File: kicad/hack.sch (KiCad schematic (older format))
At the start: 27 parts, among them P1 USB_micro, P2 CONN_01X13, P3 CONN_01X13, U1 NCP1117, U2 STF202, U3 ATSAMD21E, U4 MRF24J40MA, X1 MC-306

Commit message: Final components placement almost done
During this phase I checked if everything could fit in the board. It
didn't, so I found a replacement LDO (in a small 1.2x1.2mm DFN package)
that needs 2x0603 ceramic caps rather than two clunky electros (more
free space then) and I finally changed the D21E package to QFN as well,
now everything seems to fit quite well.
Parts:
- removed C1, C2: 10u, Capacitors_Tantalum_SMD:TantalC_SizeA_EIA-3216_HandSoldering, symbol CP_Small
- removed U1: NCP1117, hack-footprints:SOT-223, symbol NCP1117
- removed U4: MRF24J40MA, hack-footprints:MRF24J40MA, symbol MRF24J40MA
- added C1, C2: 2.2u, Capacitors_SMD:C_0603_HandSoldering, symbol C_Small
- added U1: MIC5528, Housings_DFN_QFN:DFN-6-1EP_1.2x1.2mm_Pitch0.4mm, symbol MIC5528
- C3, C4: footprint Capacitors_Tantalum_SMD:TantalC_SizeA_EIA-3216_HandSoldering -> Capacitors_SMD:c_elec_3x5.3
- U3: footprint Housings_QFP:TQFP-32_7x7mm_Pitch0.8mm -> Housings_DFN_QFN:QFN-32-1EP_5x5mm_Pitch0.5mm
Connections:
- net labels added: USB-D+, USB-D-, VDDANA, VDDCORE, shield
- net labels removed: USB-DM, USB-DP
- no-connect marks 0 -> 1
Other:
- moved on the sheet: C10, C11, C4, C6, C7, L1, L2, P2, P3, R3, R4, S1

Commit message: Layout 99,9% finished
Nets 100% routed, need to double check if copper pours are all connected
to ground; added fiducials on board (for pick-n-place machines), I only
need to find a good spot for them
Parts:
- added FID1, FID2, FID3: FIDUCIAL, hack-footprints:FIDUCIAL, symbol FIDUCIAL
- added JP1: Jumper_NO_Small, hack-footprints:SMD_Jumper, symbol Jumper_NO_Small
- added P4: CONN_01X01, Pin_Headers:Pin_Header_Straight_1x01, symbol CONN_01X01
- D1: footprint Resistors_SMD:R_0603_HandSoldering -> hack-footprints:LED_0603_HandSoldering
- L1: footprint Resistors_SMD:R_0603_HandSoldering -> hack-footprints:L_0603_HandSoldering
- U1: footprint Housings_DFN_QFN:DFN-6-1EP_1.2x1.2mm_Pitch0.4mm -> hack-footprints:DFN-6-1EP_1.2x1.2mm_Pitch0.4mm
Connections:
- net labels added: VLDO
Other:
- moved on the sheet: P2, P3

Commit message: Cleaning up before test run
Removed obsolete Eagle CAD files, added OSHW/Hackaday logos on schematic
and silkscreen, removed ground connections for pins 2-3 of 32.768 KHz
XTAL, removed traces under USB data lines, moving analog lines around
(not beneath) XTAL (w.i.p.), moved components names on silkscreen to be
readable, set fiducials in position, fixed SPST SMD package
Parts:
- added LOGO1: OSHW, hack-footprints:OSHW-LOGO, symbol OSHW
- added LOGO2: HACKADAY, hack-footprints:HACKADAY-LOGO, symbol HACKADAY
- C3, C4: footprint Capacitors_SMD:c_elec_3x5.3 -> hack-footprints:c_elec_3x5.3
- S1: footprint Buttons_Switches_SMD:SW_SPST_EVQP2 -> hack-footprints:SPST
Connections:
- wire segments 89 -> 87
- no-connect marks 1 -> 4
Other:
- moved on the sheet: C1, C10, C11, C2, C3, C4, C5, C6, C7, C8, C9, D1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

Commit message: Layout 100% completed, cosmetics not yet
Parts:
- removed X1: MC-306, hack-footprints:MC-306, symbol MC-306
- added LOGO3: HACK, hack-footprints:HACK-LOGO, symbol HACK
- added X1: ABS07, hack-footprints:xtal_3.2x1.5mm, symbol ABS07
- C6, C7: value 15p -> 10p
- S1: footprint hack-footprints:SPST -> hack-footprints:SPST-PTS_810
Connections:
- net labels added: PA02/A0, PA03/A1, PA04/A2, PA05/A3, PA06/A4, PA07/A5, PA08/0, PA09/1, PA10/2, PA11/3, PA14/4, PA15/5, PA16/6, PA17/7, PA18/8, PA19/9, PA22/10, PA23/11, PA27/12, PA28/13
- net labels removed: PA02/A, PA03/A, PA04/A, PA05/A, PA06/A, PA07/A, PA08, PA09, PA10, PA11, PA14, PA15, PA16, PA17, PA18, PA19, PA22, PA23, PA27, PA28
- wire segments 87 -> 88
- no-connect marks 4 -> 2
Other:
- moved on the sheet: R4, S1
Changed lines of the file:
@@
 LIBS:HACK
 LIBS:HiFiAudioCodecModule-cache
+LIBS:hack logo
 LIBS:hack-cache
 EELAYER 25 0
@@
 $EndComp
 $Comp
-L MC-306 X1
-U 1 1 56571094
-P 2150 1800
-F 0 "X1" H 2150 1650 60  0000 C CNN
-F 1 "MC-306" H 2150 1850 60  0000 C CNN
-F 2 "hack-footprints:MC-306" H 2150 1800 60  0001 C CNN
-F 3 "" H 2150 1800 60  0000 C CNN
-	1    2150 1800
-	1    0    0    -1
-$EndComp
-$Comp
 L R_Small R1
 U 1 1 565719DA
@@
 P 1800 2100
 F 0 "C6" H 1810 2170 50  0000 L CNN
-F 1 "15p" H 1810 2020 50  0000 L CNN
+F 1 "10p" H 1810 2020 50  0000 L CNN
 F 2 "Capacitors_SMD:C_0603_HandSoldering" H 1800 2100 60  0001 C CNN
 F 3 "" H 1800 2100 60  0000 C CNN
@@
 P 2500 2100
 F 0 "C7" H 2510 2170 50  0000 L CNN
-F 1 "15p" H 2510 2020 50  0000 L CNN
+F 1 "10p" H 2510 2020 50  0000 L CNN
 F 2 "Capacitors_SMD:C_0603_HandSoldering" H 2500 2100 60  0001 C CNN
 F 3 "" H 2500 2100 60  0000 C CNN
@@
 L R_Small R4
 U 1 1 56589A59
-P 6150 1850
-F 0 "R4" H 6180 1870 50  0000 L CNN
-F 1 "330" H 6180 1810 50  0000 L CNN
-F 2 "Resistors_SMD:R_0603_HandSoldering" H 6150 1850 60  0001 C CNN
-F 3 "" H 6150 1850 60  0000 C CNN
-	1    6150 1850
+P 6175 1850
+F 0 "R4" H 6205 1870 50  0000 L CNN
+F 1 "330" H 6205 1810 50  0000 L CNN
+F 2 "Resistors_SMD:R_0603_HandSoldering" H 6175 1850 60  0001 C CNN
+F 3 "" H 6175 1850 60  0000 C CNN
+	1    6175 1850
 	-1   0    0    -1
 $EndComp
@@
 L SPST-M S1
 U 1 1 5658420D
-P 6150 2150
-F 0 "S1" V 6150 2150 60  0000 C CNN
-F 1 "SPST-M" V 5950 2150 60  0001 C CNN
-F 2 "hack-footprints:SPST" H 6150 2150 60  0001 C CNN
-F 3 "" H 6150 2150 60  0000 C CNN
-	1    6150 2150
+P 6175 2150
+F 0 "S1" V 6175 2275 60  0000 C CNN
+F 1 "SPST-M" V 5975 2150 60  0001 C CNN
+F 2 "hack-footprints:SPST-PTS_810" H 6175 2150 60  0001 C CNN
+F 3 "" H 6175 2150 60  0000 C CNN
+	1    6175 2150
 	0    1    -1   0
 $EndComp
@@
 L GND #PWR05
 U 1 1 56587427
-P 5900 2350
-F 0 "#PWR05" H 5900 2100 50  0001 C CNN
-F 1 "GND" H 5900 2200 50  0000 C CNN
-F 2 "" H 5900 2350 60  0000 C CNN
-F 3 "" H 5900 2350 60  0000 C CNN
-	1    5900 2350
+P 5900 2400
+F 0 "#PWR05" H 5900 2150 50  0001 C CNN
+F 1 "GND" H 5900 2250 50  0000 C CNN
+F 2 "" H 5900 2400 60  0000 C CNN
+F 3 "" H 5900 2400 60  0000 C CNN
+	1    5900 2400
 	-1   0    0    -1
 $EndComp
@@
 	1    0    0    -1
 $EndComp
-Text GLabel 4850 1550 2    60   BiDi ~ 0
-PA28
-Text GLabel 5400 1750 2    60   BiDi ~ 0
-PA27
-Text GLabel 6200 1650 2    60   BiDi ~ 0
+Text GLabel 5375 1550 2    60   BiDi ~ 0
+PA28/13
+Text GLabel 4850 1750 2    60   BiDi ~ 0
+PA27/12
+Text GLabel 6225 1650 2    60   BiDi ~ 0
 !RESET
 Text GLabel 4850 2050 2    60   BiDi ~ 0
-PA23
+PA23/11
 Text GLabel 4850 2150 2    60   BiDi ~ 0
-PA22
+PA22/10
 Text GLabel 4850 2250 2    60   BiDi ~ 0
-PA19
+PA19/9
 Text GLabel 4850 2350 2    60   BiDi ~ 0
-PA18
+PA18/8
 Text GLabel 4850 2450 2    60   BiDi ~ 0
-PA17
+PA17/7
 Text GLabel 4850 2550 2    60   BiDi ~ 0
-PA16
+PA16/6
 Text GLabel 4850 850  2    60   BiDi ~ 0
 PA31/SWDIO
@@
 PA30/SWCLK
 Text GLabel 3250 2550 0    60   BiDi ~ 0
-PA15
+PA15/5
 Text GLabel 3250 2450 0    60   BiDi ~ 0
-PA14
+PA14/4
 Text GLabel 3250 2350 0    60   BiDi ~ 0
-PA11
+PA11/3
 Text GLabel 3250 2250 0    60   BiDi ~ 0
-PA10
+PA10/2
 Text GLabel 3250 2150 0    60   BiDi ~ 0
-PA09
+PA09/1
 Text GLabel 3200 2050 0    60   BiDi ~ 0
-PA08
+PA08/0
 Text GLabel 3250 1050 0    60   BiDi ~ 0
-PA02/A
+PA02/A0
 Text GLabel 3250 1150 0    60   BiDi ~ 0
-PA03/A
+PA03/A1
 Text GLabel 3250 1250 0    60   BiDi ~ 0
-PA04/A
+PA04/A2
 Text GLabel 3250 1350 0    60   BiDi ~ 0
-PA05/A
+PA05/A3
 Text GLabel 3250 1450 0    60   BiDi ~ 0
-PA06/A
+PA06/A4
 Text GLabel 3250 1550 0    60   BiDi ~ 0
-PA07/A
+PA07/A5
 $Comp
 L GND #PWR07
@@
 	5350 2300 5350 2350
 Wire Wire Line
-	6150 2300 5900 2300
-Wire Wire Line
-	5900 2250 5900 2350
+	6175 2350 5900 2350
+Wire Wire Line
+	5900 2250 5900 2400
 Wire Wire Line
 	5900 1600 5900 2050
 Connection ~ 5900 1650
-Connection ~ 5900 2300
-Wire Wire Line
-	4800 1550 4850 1550
-Wire Wire Line
-	4800 1750 5400 1750
+Connection ~ 5900 2350
+Wire Wire Line
+	4800 1550 5375 1550
+Wire Wire Line
+	4800 1750 4850 1750
 Wire Wire Line
 	4800 2050 4850 2050
@@
 	5900 1325 5900 1400
 Wire Wire Line
-	4800 1650 6200 1650
-Wire Wire Line
-	6150 1950 6150 2000
-Wire Wire Line
-	6150 1650 6150 1750
-Connection ~ 6150 1650
+	4800 1650 6225 1650
+Wire Wire Line
+	6175 1950 6175 2000
+Wire Wire Line
+	6175 1650 6175 1750
+Connection ~ 6175 1650
 Wire Wire Line
 	4800 1450 5100 1450
@@
 Text GLabel 1275 3000 0    60   Output ~ 0
 VDDF
+Text GLabel 2125 3600 0    60   BiDi ~ 0
+PA17/7
+Text GLabel 2125 3700 0    60   BiDi ~ 0
+PA18/8
+Text GLabel 2125 3800 0    60   BiDi ~ 0
+PA19/9
+Text GLabel 2125 3900 0    60   BiDi ~ 0
+PA22/10
+Text GLabel 2125 4000 0    60   BiDi ~ 0
+PA23/11
 Text GLabel 1275 3100 0    60   BiDi ~ 0
-PA17
-Text GLabel 1275 3200 0    60   BiDi ~ 0
-PA18
+PA27/12
+Text GLabel 1275 3200 0    60   Input ~ 0
+!RESET
 Text GLabel 1275 3300 0    60   BiDi ~ 0
-PA19
+PA28/13
 Text GLabel 1275 3400 0    60   BiDi ~ 0
-PA22
+PA30/SWCLK
 Text GLabel 1275 3500 0    60   BiDi ~ 0
-PA23
-Text GLabel 1275 3600 0    60   BiDi ~ 0
-PA27
-Text GLabel 1275 3700 0    60   Input ~ 0
-!RESET
-Text GLabel 1275 3800 0    60   BiDi ~ 0
-PA28
-Text GLabel 1275 3900 0    60   BiDi ~ 0
-PA30/SWCLK
-Text GLabel 1275 4000 0    60   BiDi ~ 0
 PA31/SWDIO
-Wire Wire Line
-	5350 1850 5350 1750
-Connection ~ 5350 1750
 $Comp
 L CONN_01X01 P4
@@
 Text GLabel 2300 950  2    60   Output ~ 0
 USB-D-
+Text GLabel 1275 3600 0    60   BiDi ~ 0
+PA02/A0
+Text GLabel 1275 3700 0    60   BiDi ~ 0
+PA03/A1
+Text GLabel 1275 3800 0    60   BiDi ~ 0
+PA04/A2
+Text GLabel 1275 3900 0    60   BiDi ~ 0
+PA05/A3
+Text GLabel 1275 4000 0    60   BiDi ~ 0
+PA06/A4
 Text GLabel 2125 2800 0    60   BiDi ~ 0
-PA02/A
+PA07/A5
+Text GLabel 2125 3400 0    60   BiDi ~ 0
+PA15/5
+Text GLabel 2125 3300 0    60   BiDi ~ 0
+PA14/4
+Text GLabel 2125 3200 0    60   BiDi ~ 0
+PA11/3
+Text GLabel 2125 3100 0    60   BiDi ~ 0
+PA10/2
+Text GLabel 2125 3000 0    60   BiDi ~ 0
+PA09/1
 Text GLabel 2125 2900 0    60   BiDi ~ 0
-PA03/A
-Text GLabel 2125 3000 0    60   BiDi ~ 0
-PA04/A
-Text GLabel 2125 3100 0    60   BiDi ~ 0
-PA05/A
-Text GLabel 2125 3200 0    60   BiDi ~ 0
-PA06/A
-Text GLabel 2125 3300 0    60   BiDi ~ 0
-PA07/A
-Text GLabel 2125 3900 0    60   BiDi ~ 0
-PA15
-Text GLabel 2125 3800 0    60   BiDi ~ 0
-PA14
-Text GLabel 2125 3700 0    60   BiDi ~ 0
-PA11
-Text GLabel 2125 3600 0    60   BiDi ~ 0
-PA10
+PA08/0
 Text GLabel 2125 3500 0    60   BiDi ~ 0
-PA09
-Text GLabel 2125 3400 0    60   BiDi ~ 0
-PA08
-Text GLabel 2125 4000 0    60   BiDi ~ 0
-PA16
+PA16/6
 Text GLabel 1275 4225 0    60   Output ~ 0
 VDDANA
@@
 	1    0    0    -1
 $EndComp
-NoConn ~ 2050 2150
-NoConn ~ 2250 2150
 NoConn ~ 1350 1150
 $Comp
 L OSHW LOGO1
 U 1 1 56815E8B
-P 4475 3400
-F 0 "LOGO1" H 4475 3060 60  0001 C CNN
-F 1 "OSHW" H 4475 3740 60  0001 C CNN
-F 2 "hack-footprints:OSHW-LOGO" H 4475 3400 60  0001 C CNN
-F 3 "" H 4475 3400 60  0000 C CNN
-	1    4475 3400
+P 5800 3750
+F 0 "LOGO1" H 5800 3410 60  0001 C CNN
+F 1 "OSHW" H 5800 4090 60  0001 C CNN
+F 2 "hack-footprints:OSHW-LOGO" H 5800 3750 60  0001 C CNN
+F 3 "" H 5800 3750 60  0000 C CNN
+	1    5800 3750
 	1    0    0    -1
 $EndComp
@@
 L HACKADAY LOGO2
 U 1 1 56815EDD
-P 5325 3300
-F 0 "LOGO2" H 5325 3118 60  0001 C CNN
-F 1 "HACKADAY" H 5325 3482 60  0001 C CNN
-F 2 "hack-footprints:HACKADAY-LOGO" H 5325 3300 60  0001 C CNN
-F 3 "" H 5325 3300 60  0000 C CNN
-	1    5325 3300
-	1    0    0    -1
-$EndComp
+P 4450 3725
+F 0 "LOGO2" H 4450 3543 60  0001 C CNN
+F 1 "HACKADAY" H 4450 3907 60  0001 C CNN
+F 2 "hack-footprints:HACKADAY-LOGO" H 4450 3725 60  0001 C CNN
+F 3 "" H 4450 3725 60  0000 C CNN
+	1    4450 3725
+	1    0    0    -1
+$EndComp
+$Comp
+L ABS07 X1
+U 1 1 56825CA1
+P 2150 1800
+F 0 "X1" H 2150 1650 60  0000 C CNN
+F 1 "ABS07" H 2150 1850 60  0000 C CNN
+F 2 "hack-footprints:xtal_3.2x1.5mm" H 2150 1800 60  0001 C CNN
+F 3 "" H 2150 1800 60  0000 C CNN
+	1    2150 1800
+	1    0    0    -1
+$EndComp
+$Comp
+L HACK LOGO3
+U 1 1 56825DB6
+P 5125 3125
+F 0 "LOGO3" H 5125 2905 60  0001 C CNN
+F 1 "HACK" H 5125 3345 60  0001 C CNN
+F 2 "hack-footprints:HACK-LOGO" H 5125 3125 60  0001 C CNN
+F 3 "" H 5125 3125 60  0000 C CNN
+	1    5125 3125
+	1    0    0    -1
+$EndComp
+Wire Wire Line
+	6175 2350 6175 2300
+Wire Wire Line
+	5350 1850 5350 1550
+Connection ~ 5350 1550
 $EndSCHEMATC

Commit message: Changed USB connector package, revised layout
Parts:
- P1: footprint hack-footprints:47346-0001 -> hack-footprints:ST-USB-001G
- P2, P3: footprint Pin_Headers:Pin_Header_Straight_1x13 -> hack-footprints:Pin_Castellated_1x13
- P4: footprint Pin_Headers:Pin_Header_Straight_1x01 -> hack-footprints:Pin_Castellated_1x01
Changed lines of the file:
@@
 F 0 "P1" H 950 750 60  0000 C CNN
 F 1 "USB_micro" H 950 650 60  0000 C CNN
-F 2 "hack-footprints:47346-0001" H 950 700 60  0001 C CNN
+F 2 "hack-footprints:ST-USB-001G" H 950 700 60  0001 C CNN
 F 3 "" H 950 700 60  0000 C CNN
 	1    950  700
@@
 F 0 "P2" H 1475 4100 50  0000 C CNN
 F 1 "CONN_01X13" V 1575 3400 50  0000 C CNN
-F 2 "Pin_Headers:Pin_Header_Straight_1x13" H 1475 3400 60  0001 C CNN
+F 2 "hack-footprints:Pin_Castellated_1x13" H 1475 3400 60  0001 C CNN
 F 3 "" H 1475 3400 60  0000 C CNN
 	1    1475 3400
@@
 F 0 "P3" H 2325 4100 50  0000 C CNN
 F 1 "CONN_01X13" V 2425 3400 50  0000 C CNN
-F 2 "Pin_Headers:Pin_Header_Straight_1x13" H 2325 3400 60  0001 C CNN
+F 2 "hack-footprints:Pin_Castellated_1x13" H 2325 3400 60  0001 C CNN
 F 3 "" H 2325 3400 60  0000 C CNN
 	1    2325 3400
@@
 F 0 "P4" H 1475 4325 50  0000 C CNN
 F 1 "CONN_01X01" V 1575 4225 50  0000 C CNN
-F 2 "Pin_Headers:Pin_Header_Straight_1x01" H 1475 4225 60  0001 C CNN
+F 2 "hack-footprints:Pin_Castellated_1x01" H 1475 4225 60  0001 C CNN
 F 3 "" H 1475 4225 60  0000 C CNN
 	1    1475 4225

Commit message: fresh PDF and Gerbers in separate folders. Step/VRML files ready for 3D render
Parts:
- C1, C2: value 2.2u -> 2.2uF; footprint Capacitors_SMD:C_0603_HandSoldering -> hack:C_0603_HandSoldering
- C10, C11, C8, C9: value 100n -> 100nF; footprint Capacitors_SMD:C_0603_HandSoldering -> hack:C_0603_HandSoldering
- C3, C4: value 10u -> 10uF; footprint hack-footprints:c_elec_3x5.3 -> hack:c_elec_3x5.3
- C5: value 4.5n -> 4.5nF; footprint Capacitors_SMD:C_0603_HandSoldering -> hack:C_0603_HandSoldering
- C6, C7: value 10p -> 10pF; footprint Capacitors_SMD:C_0603_HandSoldering -> hack:C_0603_HandSoldering
- D1: footprint hack-footprints:LED_0603_HandSoldering -> hack:LED_0603_HandSoldering
- FID1, FID2, FID3: footprint hack-footprints:FIDUCIAL -> hack:FIDUCIAL
- JP1: footprint hack-footprints:SMD_Jumper -> hack:SMD_Jumper
- L1: footprint hack-footprints:L_0603_HandSoldering -> hack:L_0603_HandSoldering
- L2: value 10u -> 10uH; footprint hack-footprints:ELLVFG -> hack:ELLVFG
- LOGO1: footprint hack-footprints:OSHW-LOGO -> hack:OSHW-LOGO; manf# (none) -> mfr_pn
- LOGO2: footprint hack-footprints:HACKADAY-LOGO -> hack:HACKADAY-LOGO; manf# (none) -> mfr_pn
- LOGO3: footprint hack-footprints:HACK-LOGO -> (none); manf# (none) -> Value
- P1: footprint hack-footprints:ST-USB-001G -> hack:47346-0001
- R1, R2, R4: footprint Resistors_SMD:R_0603_HandSoldering -> hack:R_0603_HandSoldering
- R3: value 10K -> 10k; footprint Resistors_SMD:R_0603_HandSoldering -> hack:R_0603_HandSoldering
- S1: value SPST-M -> RST
- U1: footprint hack-footprints:DFN-6-1EP_1.2x1.2mm_Pitch0.4mm -> hack:DFN-6-1EP_1.2x1.2mm_Pitch0.4mm
- U2: footprint hack-footprints:TSOP-6 -> hack:TSOP-6
- U3: footprint Housings_DFN_QFN:QFN-32-1EP_5x5mm_Pitch0.5mm -> hack:QFN-32-1EP_5x5mm_Pitch0.5mm
- X1: footprint hack-footprints:xtal_3.2x1.5mm -> (none)
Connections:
- no-connect marks 2 -> 4
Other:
- note added: "BREAKOUT PINS + CASTELLATED EDGES"
- note added: "CRYSTAL"
- note added: "JUMPER"
- note added: "MICRO CONTROLLER"
- note added: "USB_IN + FILTER"
- note added: "V_REG"
- moved on the sheet: C1, C10, C11, C2, C3, C4, C5, C6, C7, C8, C9, D1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

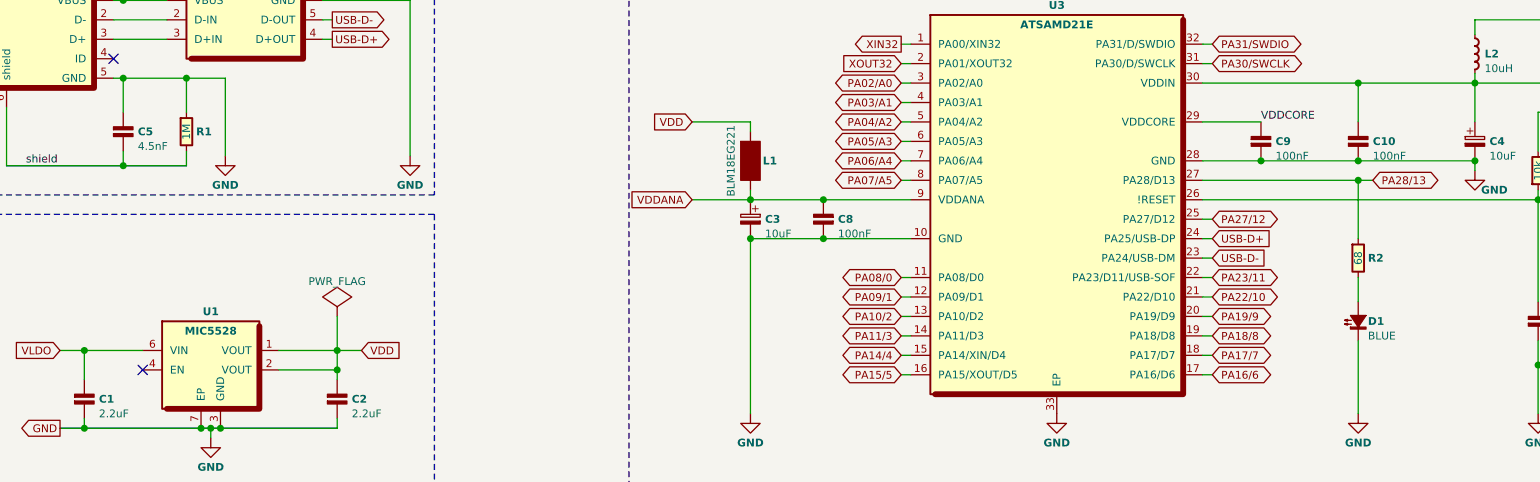
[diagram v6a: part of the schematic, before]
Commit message: Added datasheets, manufacturer numbers field for every component
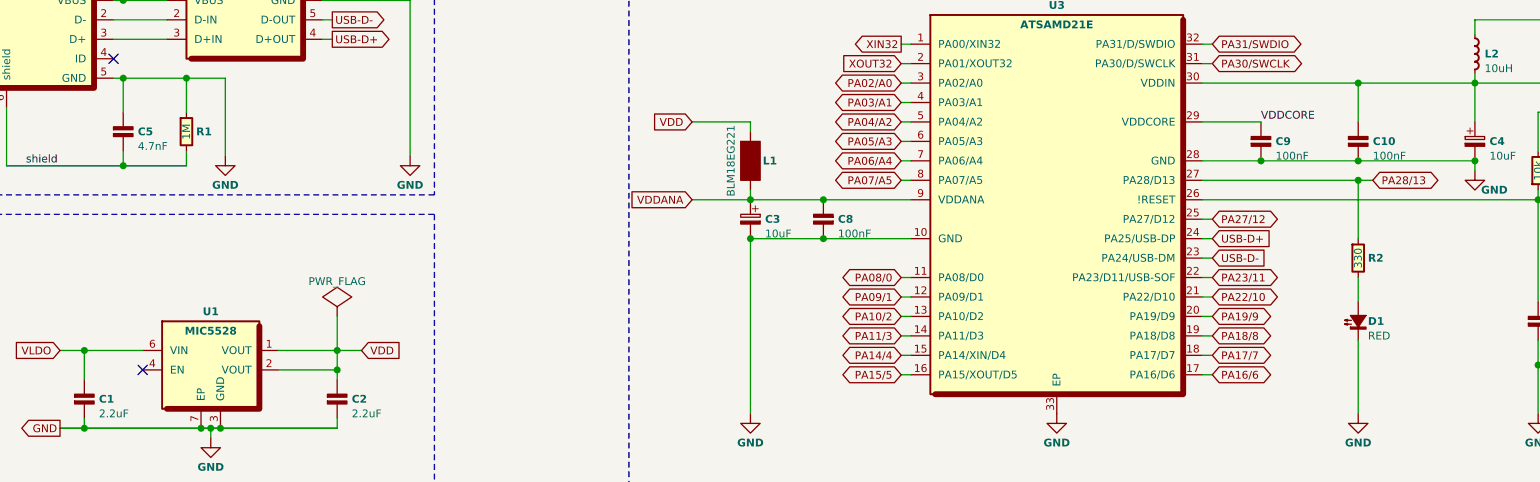
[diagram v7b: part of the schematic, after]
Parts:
- C1: manf# (none) -> 302010054
- C3: manf# (none) -> UWX1C100MCL2GB
- C5: value 4.5nF -> 4.7nF; manf# (none) -> 302010144
- C6: manf# (none) -> 302010097
- C8: manf# (none) -> 302010138
- D1: value BLUE -> RED; manf# (none) -> 304090042
- R1: manf# (none) -> 301010151
- R2: value 68 -> 330; manf# (none) -> 301010300
- R3: manf# (none) -> 301010299
- S1: manf# (none) -> 311020045
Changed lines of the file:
@@
 F 1 "1M" V 2025 1975 40  0000 C CNN
 F 2 "hack:R_0603_HandSoldering" H 2025 1975 40  0001 C CNB
-F 3 "" H 2025 1975 40  0000 C CNB
+F 3 "https://github.com/MickMad/HACK/tree/master/kicad/datasheets/301010151.pdf" H 2025 1975 40  0001 C CNB
+F 4 "301010151" H 2025 1975 60  0001 C CNN "manf#"
 	1    2025 1975
 	1    0    0    -1
@@
 P 1700 1975
 F 0 "C5" H 1775 1975 40  0000 L CNB
-F 1 "4.5nF" H 1775 1900 40  0000 L CNN
+F 1 "4.7nF" H 1775 1900 40  0000 L CNN
 F 2 "hack:C_0603_HandSoldering" H 1700 1975 40  0001 C CNB
-F 3 "" H 1700 1975 40  0000 C CNB
+F 3 "https://github.com/MickMad/HACK/tree/master/kicad/datasheets/0100850P1.pdf" H 1700 1975 40  0001 C CNB
+F 4 "302010144" H 1700 1975 60  0001 C CNN "manf#"
 	1    1700 1975
 	1    0    0    -1
@@
 F 1 "10pF" H 1575 4275 40  0000 L CNN
 F 2 "hack:C_0603_HandSoldering" H 1500 4350 40  0001 C CNB
-F 3 "" H 1500 4350 40  0000 C CNB
+F 3 "https://github.com/MickMad/HACK/tree/master/kicad/datasheets/302010097.pdf" H 1500 4350 40  0001 C CNB
+F 4 "302010097" H 1500 4350 60  0001 C CNN "manf#"
 	1    1500 4350
 	1    0    0    -1
@@
 F 1 "10uF" H 4850 2350 40  0000 R CNN
 F 2 "hack:c_elec_3x5.3" H 4925 2425 40  0001 C CNB
-F 3 "" H 4925 2425 40  0000 C CNB
+F 3 "https://github.com/MickMad/HACK/tree/master/kicad/datasheets/e-wx-11809.pdf" H 4925 2425 40  0001 C CNB
+F 4 "UWX1C100MCL2GB" H 4925 2425 60  0001 C CNN "manf#"
 	1    4925 2425
 	-1   0    0    -1
@@
 F 1 "100nF" H 5225 2350 40  0000 R CNN
 F 2 "hack:C_0603_HandSoldering" H 5300 2425 40  0001 C CNB
-F 3 "" H 5300 2425 40  0000 C CNB
+F 3 "https://github.com/MickMad/HACK/tree/master/kicad/datasheets/0100020P1.pdf" H 5300 2425 40  0001 C CNB
+F 4 "302010138" H 5300 2425 60  0001 C CNN "manf#"
 	1    5300 2425
 	-1   0    0    -1
@@
 P 8050 2950
 F 0 "D1" V 8050 2900 40  0000 R CNB
-F 1 "BLUE" V 7975 2900 40  0000 R CNN
+F 1 "RED" V 7975 2900 40  0000 R CNN
 F 2 "hack:LED_0603_HandSoldering" V 8050 2950 40  0001 C CNB
-F 3 "" V 8050 2950 40  0000 C CNB
+F 3 "https://github.com/MickMad/HACK/tree/master/kicad/datasheets/0330020P1.pdf" V 8050 2950 40  0001 C CNB
+F 4 "304090042" V 8050 2950 60  0001 C CNN "manf#"
 	1    8050 2950
 	0    -1   -1   0
@@
 P 8050 2625
 F 0 "R2" H 8100 2625 40  0000 L CNB
-F 1 "68" V 8050 2625 40  0000 C CNN
+F 1 "330" V 8050 2625 40  0000 C CNN
 F 2 "hack:R_0603_HandSoldering" H 8050 2625 40  0001 C CNB
-F 3 "" H 8050 2625 40  0000 C CNB
+F 3 "https://github.com/MickMad/HACK/tree/master/kicad/datasheets/0011330P1.pdf" H 8050 2625 40  0001 C CNB
+F 4 "301010300" H 8050 2625 60  0001 C CNN "manf#"
 	1    8050 2625
 	1    0    0    -1
@@
 F 1 "RST" V 9275 3125 40  0000 L CNN
 F 2 "hack-footprints:SPST-PTS_810" H 9350 2950 40  0001 C CNB
-F 3 "" H 9350 2950 40  0000 C CNB
+F 3 "https://github.com/MickMad/HACK/tree/master/kicad/datasheets/311020045.pdf" H 9350 2950 40  0001 C CNB
+F 4 "311020045" V 9350 2950 60  0001 C CNN "manf#"
 	1    9350 2950
 	0    1    -1   0
@@
 F 1 "10k" V 8975 2175 40  0000 C CNN
 F 2 "hack:R_0603_HandSoldering" H 8975 2175 40  0001 C CNB
-F 3 "" H 8975 2175 40  0000 C CNB
+F 3 "https://github.com/MickMad/HACK/tree/master/kicad/datasheets/0011240P1.pdf" H 8975 2175 40  0001 C CNB
+F 4 "301010299" H 8975 2175 60  0001 C CNN "manf#"
 	1    8975 2175
 	1    0    0    1
@@
 F 1 "2.2uF" H 1575 3275 40  0000 L CNN
 F 2 "hack:C_0603_HandSoldering" H 1500 3350 40  0001 C CNB
-F 3 "" H 1500 3350 40  0000 C CNB
+F 3 "https://github.com/MickMad/HACK/tree/master/kicad/datasheets/302010054.pdf" H 1500 3350 40  0001 C CNB
+F 4 "302010054" H 1500 3350 60  0001 C CNN "manf#"
 	1    1500 3350
 	1    0    0    -1
